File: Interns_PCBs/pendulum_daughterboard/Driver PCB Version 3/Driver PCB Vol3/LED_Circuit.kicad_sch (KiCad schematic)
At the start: 40 parts, among them J4 Conn_01x04, U1 4081, U2 4011, U3 4011, U4 4071

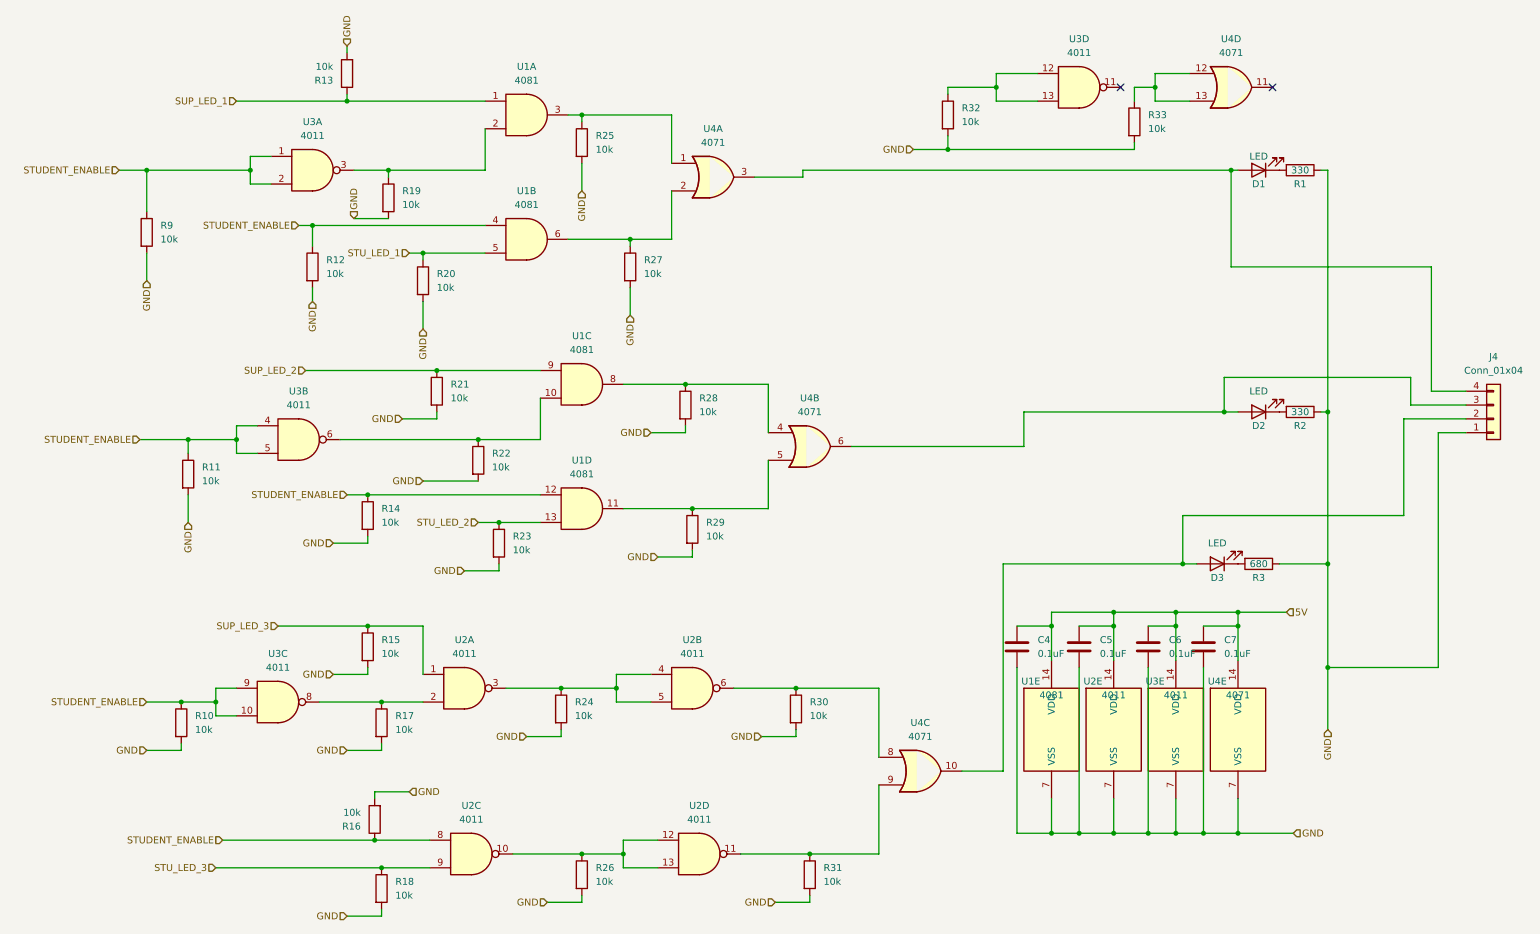
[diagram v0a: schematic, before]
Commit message: Flipped Diode on schematic
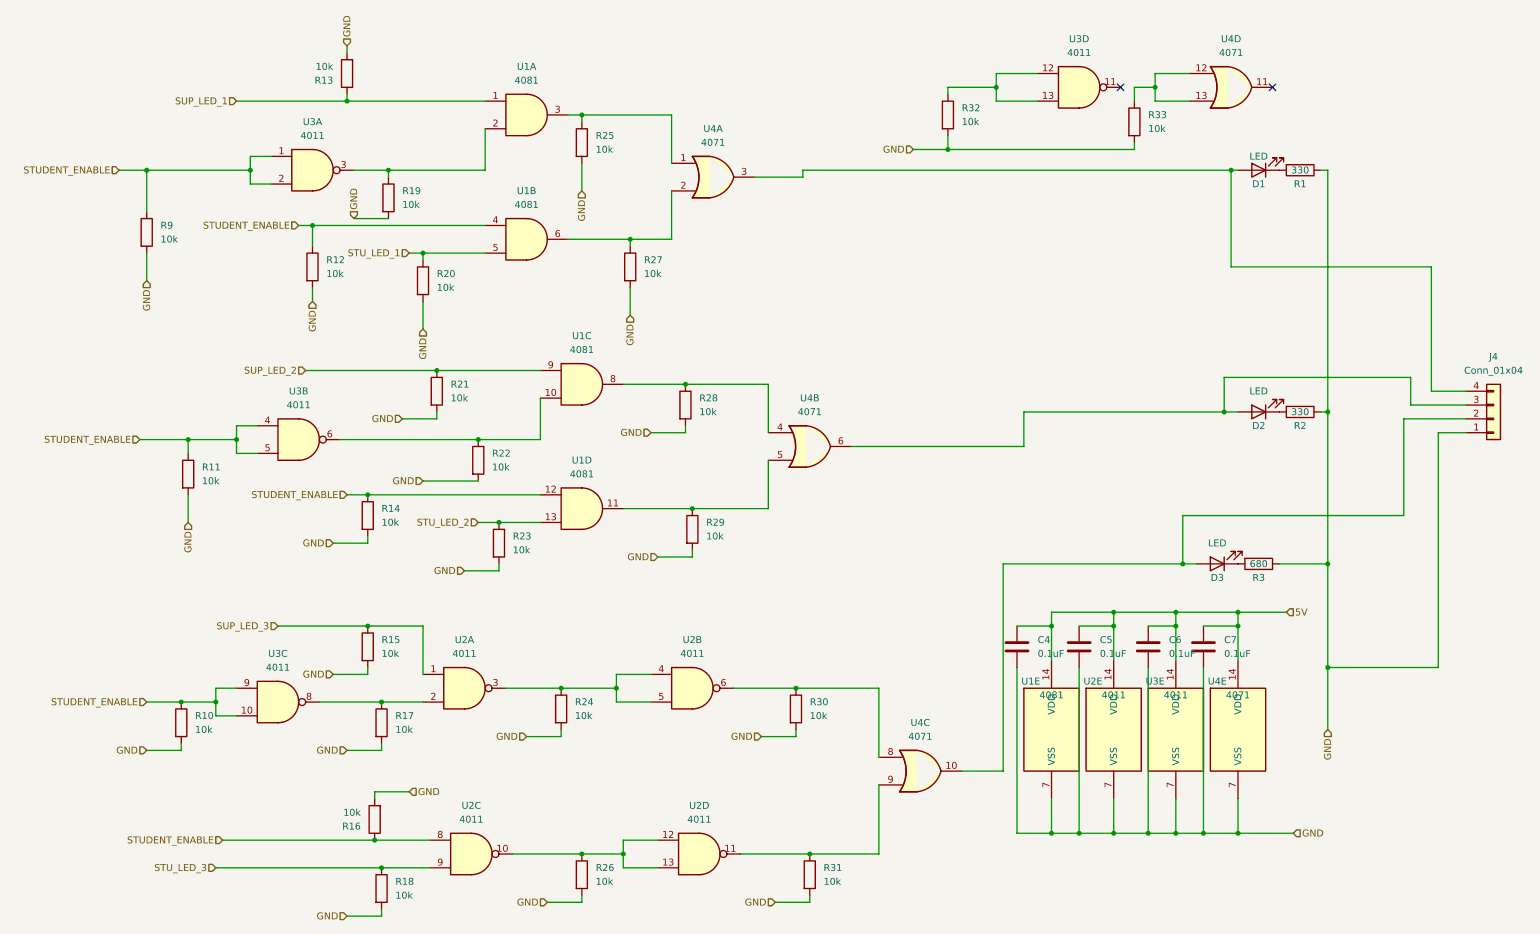
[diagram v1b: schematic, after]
